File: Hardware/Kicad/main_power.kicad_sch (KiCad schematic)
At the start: 13 parts, among them J1 5V_to_Rail_and_ESP_32_Proto_b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, J10 Edge Pads Right (GND), J14 5V LED Strips Long Side Rail, J16 GND Long Side Rail, J26 5V/GND from Power Board, J6 5V_15A_Power, J9 Edge Pads Left (5V), P1 IEC_60320_C13_Plug

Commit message: Replaced 1602 to 2004 in Kicad and Tinkercad
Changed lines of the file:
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@@
 	(text "MAIN POWER"
 		(exclude_from_sim no)
-		(at 130.048 19.812 0)
+		(at 105.664 22.098 0)
 		(effects
 			(font
@@
 		)
 	)
+	(polyline
+		(pts
+			(xy 11.43 140.97) (xy 200.66 140.97)
+		)
+		(stroke
+			(width 0)
+			(type default)
+		)
+	)
 	(wire
 		(pts
@@
 		)
 	)
+	(polyline
+		(pts
+			(xy 11.43 110.49) (xy 200.66 110.49)
+		)
+		(stroke
+			(width 0)
+			(type default)
+		)
+	)
 	(wire
 		(pts
@@
 		)
 		(stroke
+			(width 0)
+			(type default)
+		)
+	)
+	(polyline
+		(pts
+			(xy 8.89 25.4) (xy 198.12 25.4)
+		)
+		(stroke

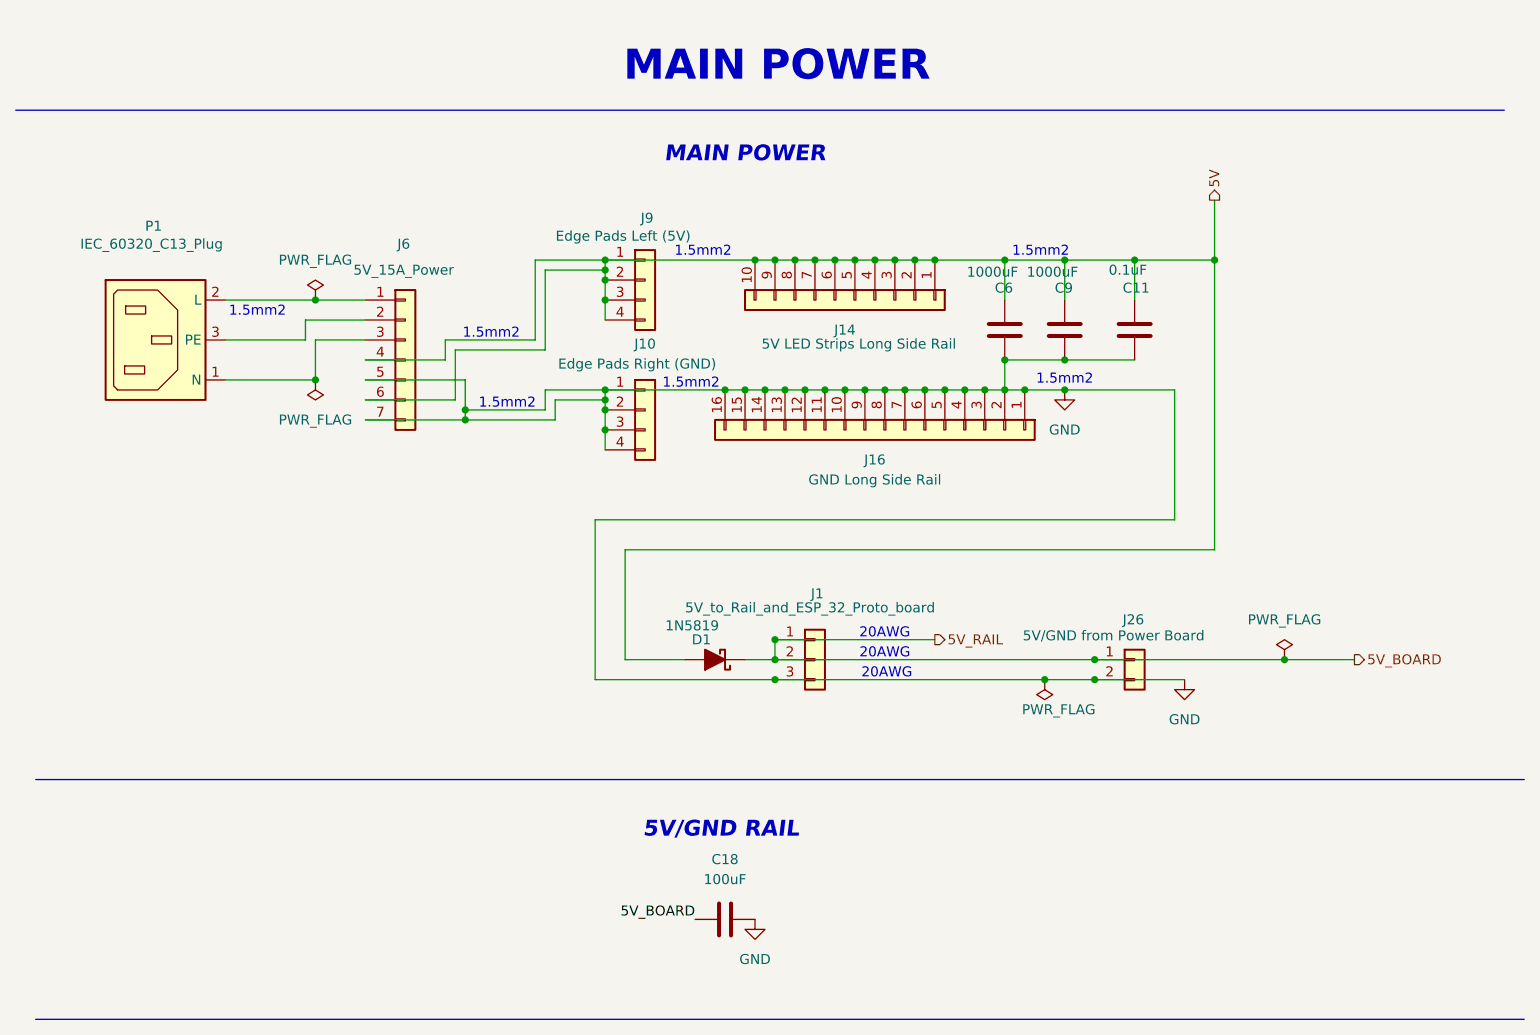
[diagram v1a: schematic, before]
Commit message: Added Kicad proto board
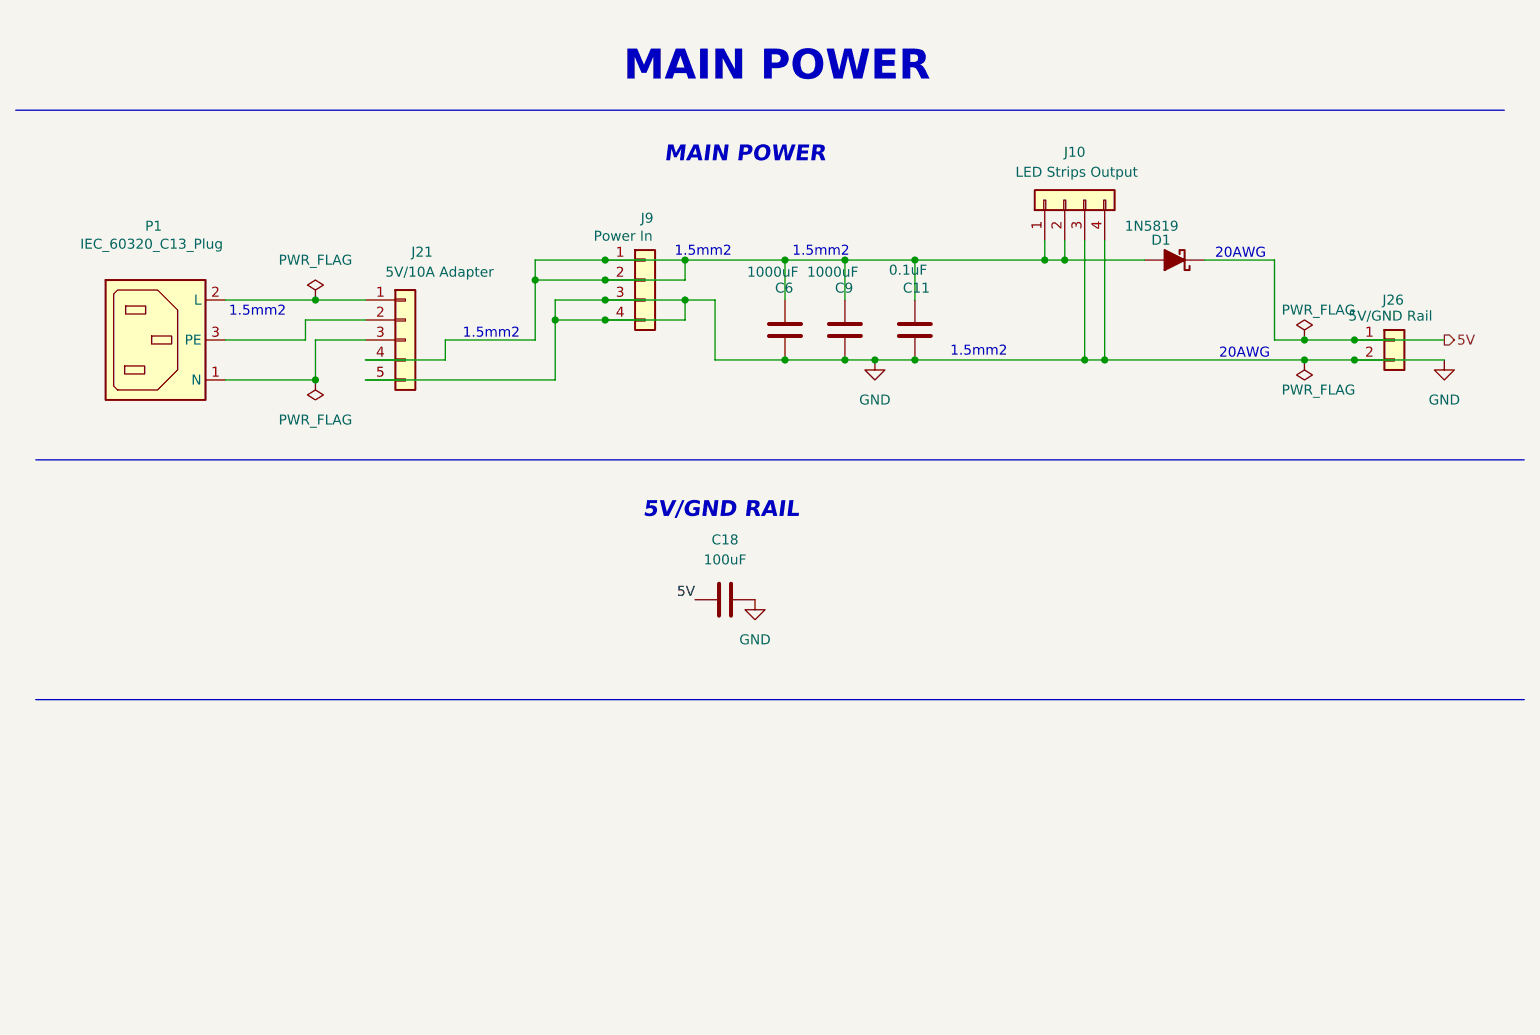
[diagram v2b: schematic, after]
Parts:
- removed J1: 5V_to_Rail_and_ESP_32_Proto_board, PCM_SparkFun-Connector:ScrewTerminal_1x03_P5.0mm, symbol Connector_Generic:Conn_01x03
- removed J14: 5V LED Strips Long Side Rail, Connector_PinHeader_2.54mm:PinHeader_1x10_P2.54mm_Vertical_SMD_Pin1Left, symbol Connector_Generic:Conn_01x10
- removed J16: GND Long Side Rail, Connector_PinHeader_2.54mm:PinHeader_1x16_P2.54mm_Vertical_SMD_Pin1Left, symbol Connector_Generic:Conn_01x16
- removed J6: 5V_15A_Power, Connector_PinSocket_2.54mm:PinSocket_1x07_P2.54mm_Vertical, symbol Connector_Generic:Conn_01x07
- added J21: 5V/10A Adapter, Connector_FFC-FPC:Amphenol_F32Q-1A7x1-11005_1x05-1MP_P0.5mm_Horizontal, symbol Connector_Generic:Conn_01x05
- C11: footprint Capacitor_THT:C_Disc_D3.0mm_W1.6mm_P2.50mm -> Capacitor_SMD:C_0805_2012Metric_Pad1.18x1.45mm_HandSolder
- D1: footprint PCM_Diode_THT_AKL:D_DO-41_SOD81_P7.62mm_Horizontal -> Diode_SMD:D_SOD-123
- J10: value Edge Pads Right (GND) -> LED Strips Output; footprint Connector_PinSocket_2.54mm:PinSocket_1x04_P2.54mm_Vertical_SMD_Pin1Left -> TerminalBlock_Phoenix:TerminalBlock_Phoenix_MKDS-1,5-4_1x04_P5.00mm_Horizontal
- J26: value 5V/GND from Power Board -> 5V/GND Rail; footprint PCM_SparkFun-Connector:ScrewTerminal_1x02_P5.0mm -> TerminalBlock_Phoenix:TerminalBlock_Phoenix_MKDS-1,5-2_1x02_P5.00mm_Horizontal
- J9: value Edge Pads Left (5V) -> Power In; footprint Connector_PinSocket_2.54mm:PinSocket_1x04_P2.54mm_Vertical_SMD_Pin1Left -> TerminalBlock_Phoenix:TerminalBlock_Phoenix_MKDS-1,5-4_1x04_P5.00mm_Horizontal
- P1: footprint Connector_PinHeader_2.54mm:PinHeader_1x03_P2.54mm_Vertical -> (none)
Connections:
- net 5V_BOARD is gone; now on net 5V: C18.1, D1.1 (K), J26.1 (Pin_1)
- net 5V: no longer C11.2, C6.2, C9.2, D1.2 (A), J9.1 (Pin_1), J9.2 (Pin_2), J9.3 (Pin_3), J9.4 (Pin_4)
- net GND: now also J9.3 (Pin_3), J9.4 (Pin_4), J21.5 (Pin_5); no longer J10.1 (Pin_1), J10.2 (Pin_2)
- net at P1.2 (L): now also J21.1 (Pin_1)
- net at P1.3 (PE): now also J21.2 (Pin_2)
- net at P1.1 (N): now also J21.3 (Pin_3)
- new net: C11.2, C6.2, C9.2, D1.2 (A), J10.1 (Pin_1), J10.2 (Pin_2), J21.4 (Pin_4), J9.1 (Pin_1), J9.2 (Pin_2)
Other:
- moved on the sheet: C11, C18, C6, C9, D1, J10, J26

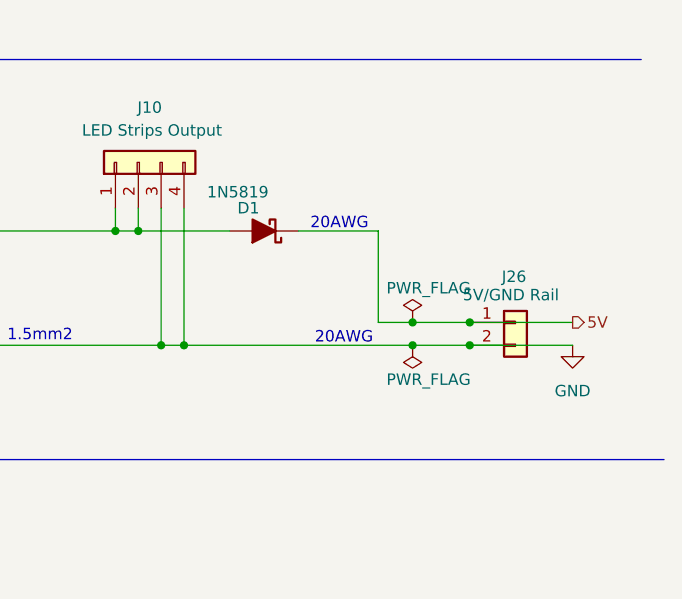
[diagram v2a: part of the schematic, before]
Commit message: New Fraxis PCB layout
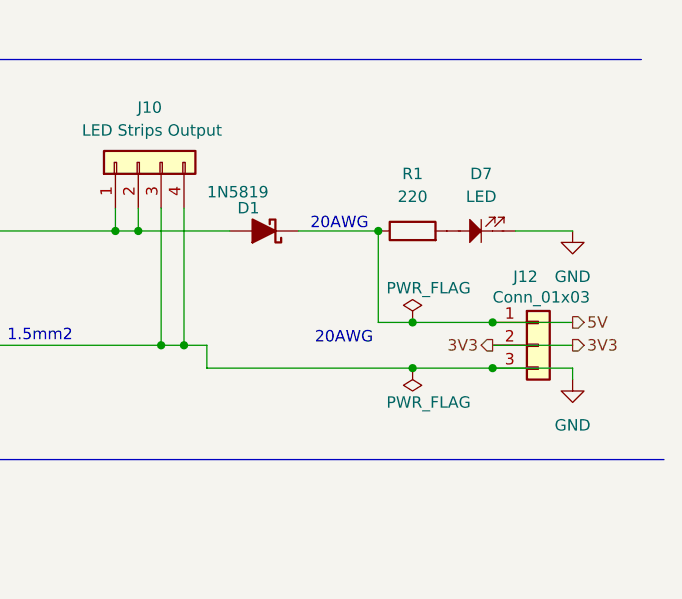
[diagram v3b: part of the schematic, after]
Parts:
- removed J26: 5V/GND Rail, TerminalBlock_Phoenix:TerminalBlock_Phoenix_MKDS-1,5-2_1x02_P5.00mm_Horizontal, symbol PCM_4ms_Connector:Conn_01x02
- added D7: LED, LED_SMD:LED_0805_2012Metric_Pad1.15x1.40mm_HandSolder, symbol PCM_SL_Devices:LED
- added J12: Conn_01x03, TerminalBlock_Phoenix:TerminalBlock_Phoenix_MKDS-1,5-3_1x03_P5.00mm_Horizontal, symbol PCM_4ms_Connector:Conn_01x03
- added R1: 220, PCM_Resistor_SMD_AKL:R_0805_2012Metric_Pad1.20x1.40mm_HandSolder, symbol Device:R
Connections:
- net 5V: now also J12.1 (Pin_1), R1.1
- net GND: now also D7.1, J12.3 (Pin_3)
- new net: D7.2, R1.2
- new net 3V3: J12.2 (Pin_2)

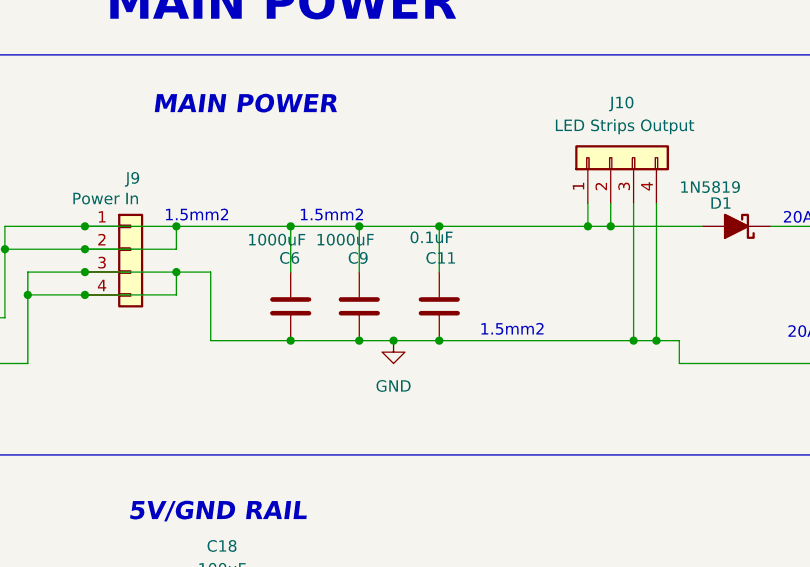
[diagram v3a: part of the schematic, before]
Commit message: Added safety in Kicad power, added NVS read version/tm1637 brightness
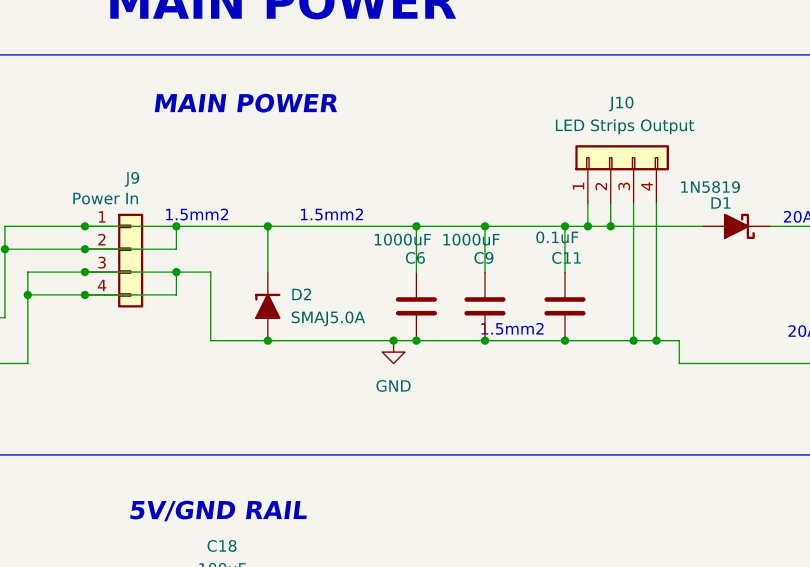
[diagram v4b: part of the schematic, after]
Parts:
- added D2: SMAJ5.0A, PCM_Diode_SMD_AKL:D_SMA, symbol PCM_Diode_TVS_AKL:SMAJ5.0A
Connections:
- net GND: now also D2.2 (A)
- net at C11.2, C6.2, C9.2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: now also D2.1 (K)
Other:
- moved on the sheet: C11, C6, C9
